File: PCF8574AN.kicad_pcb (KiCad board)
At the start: 2 copper layers, 8 parts, among them J1 Conn_01x04, J2 Conn_01x03, J3 Conn_01x10, J4 Conn_01x04, U1 PCF8574

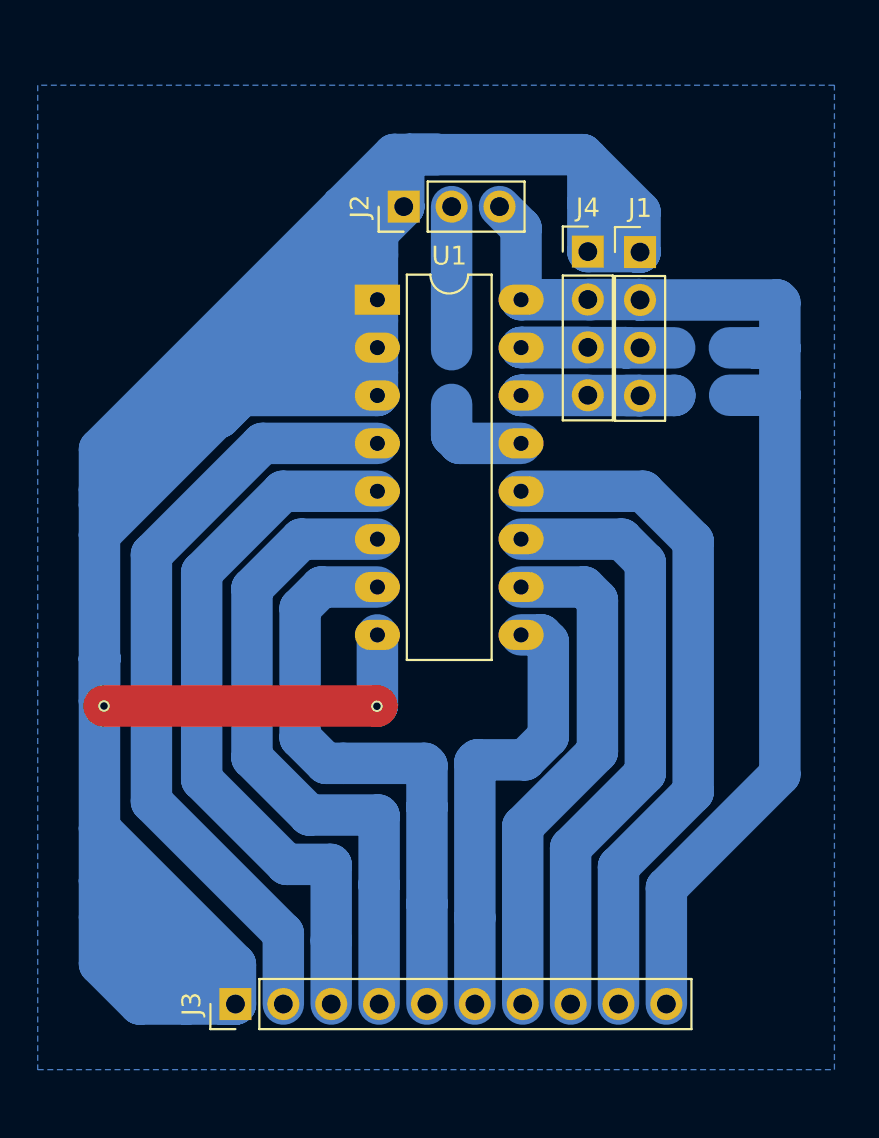
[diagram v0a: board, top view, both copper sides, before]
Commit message: Migrate project to new Kicad version. Adding headers for change address of chip PCF8574.
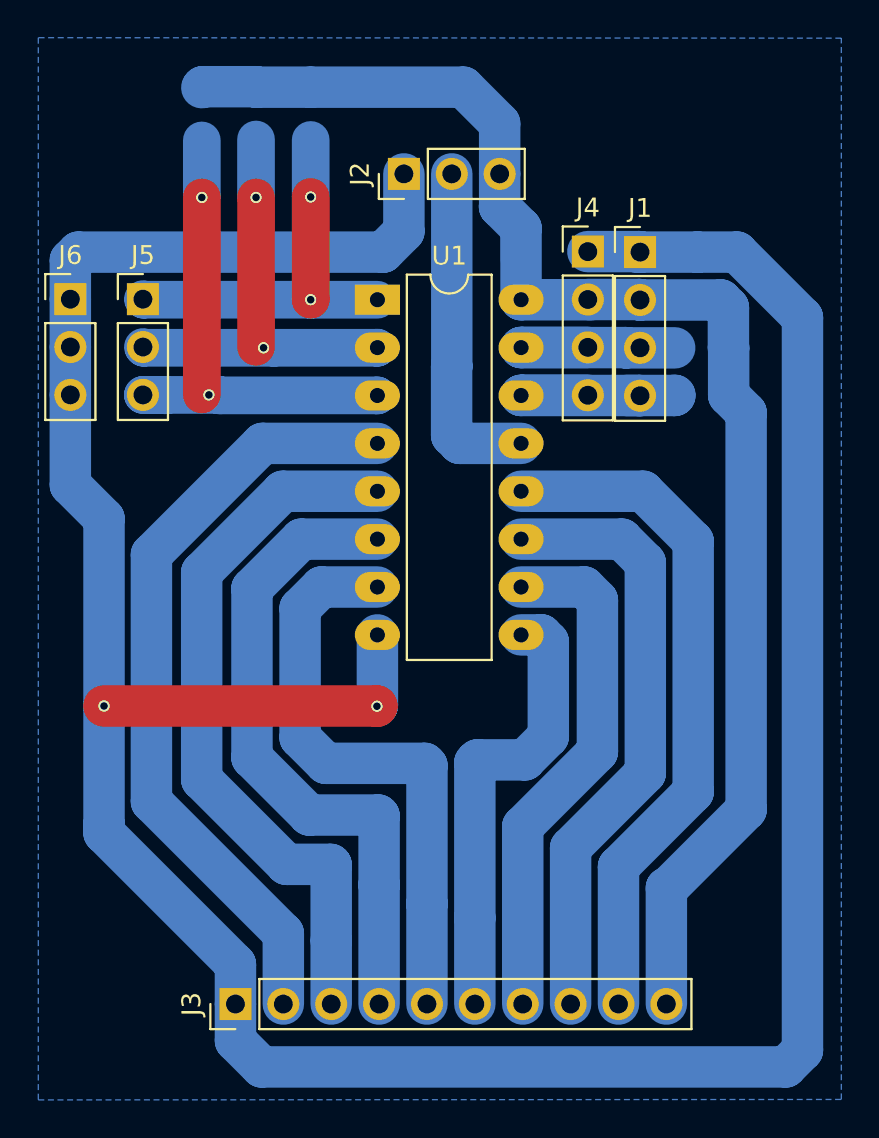
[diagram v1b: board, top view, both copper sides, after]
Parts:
- added J5: Conn_01x03_Male, Connector_PinHeader_2.54mm:PinHeader_1x03_P2.54mm_Vertical, F.Cu at (37.7, 34.9)
- added J6: Conn_01x03_Male, Connector_PinHeader_2.54mm:PinHeader_1x03_P2.54mm_Vertical, F.Cu at (33.9, 34.9)
- added R4: R, Resistor_SMD:R_1206_3216Metric, B.Cu at (40.8, 25.1)
- added R5: R, Resistor_SMD:R_1206_3216Metric, B.Cu at (43.7, 25.1)
- added R6: R, Resistor_SMD:R_1206_3216Metric, B.Cu at (46.6, 25.1)
- J1, J4: value Conn_01x04 -> Conn_01x04_Male; footprint Pin_Headers:Pin_Header_Straight_1x04_Pitch2.54mm -> Connector_PinHeader_2.54mm:PinHeader_1x04_P2.54mm_Vertical
- J2: value Conn_01x03 -> Conn_01x03_Male; footprint Pin_Headers:Pin_Header_Straight_1x03_Pitch2.54mm -> Connector_PinHeader_2.54mm:PinHeader_1x03_P2.54mm_Vertical
- J3: value Conn_01x10 -> Conn_01x10_Male; footprint Pin_Headers:Pin_Header_Straight_1x10_Pitch2.54mm -> Connector_PinHeader_2.54mm:PinHeader_1x10_P2.54mm_Vertical
- R1, R2: value 2.2k -> R; footprint Resistors_SMD:R_1206 -> Resistor_SMD:R_1206_3216Metric
- R3: footprint Resistors_SMD:R_1206 -> Resistor_SMD:R_1206_3216Metric
- U1: footprint Housings_DIP:DIP-16_W7.62mm_LongPads -> Package_DIP:DIP-16_W7.62mm_LongPads
- moved R3 7.02 mm to (55.9, 32.3), turned to 180 degrees
- moved J2 1.74 mm to (51.5, 28.3)
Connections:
- R3 pad 1: Net-(R3-Pad1) -> +5V
- U1 pad 1: GND -> Net-(J5-Pad1)
- U1 pad 13: Net-(R3-Pad1) -> Net-(J2-Pad2)
- U1 pad 2: GND -> Net-(J5-Pad2)
- U1 pad 3: GND -> Net-(J5-Pad3)
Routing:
- net GND: track 239.2 -> 167.6 mm
- net Net-(J5-Pad3): track 0.00 -> 27.2 mm, vias 0 -> 2
- net Net-(J5-Pad2): track 0.00 -> 23.5 mm, vias 0 -> 2
- net Net-(J5-Pad1): track 0.00 -> 20.9 mm, vias 0 -> 2
- net +5V: track 65.5 -> 76.9 mm
- net Net-(J2-Pad2): track 7.59 -> 17.7 mm
- net Net-(R3-Pad1): track 5.51 -> 0.00 mm
